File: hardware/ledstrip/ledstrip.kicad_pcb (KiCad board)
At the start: 4 copper layers, 98 parts, among them J1 Conn_ARM_JTAG_SWD_10, J2 USB_C_Receptacle_USB2.0_16P, J4 BMS connectors, J5 Ledstrip connector, J6 Header for STUSB4500 I2C, Q1 Q_NMOS, Q10 Q_PMOS, Q2 Q_NMOS, Q3 Q_NMOS, Q4 Q_PMOS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

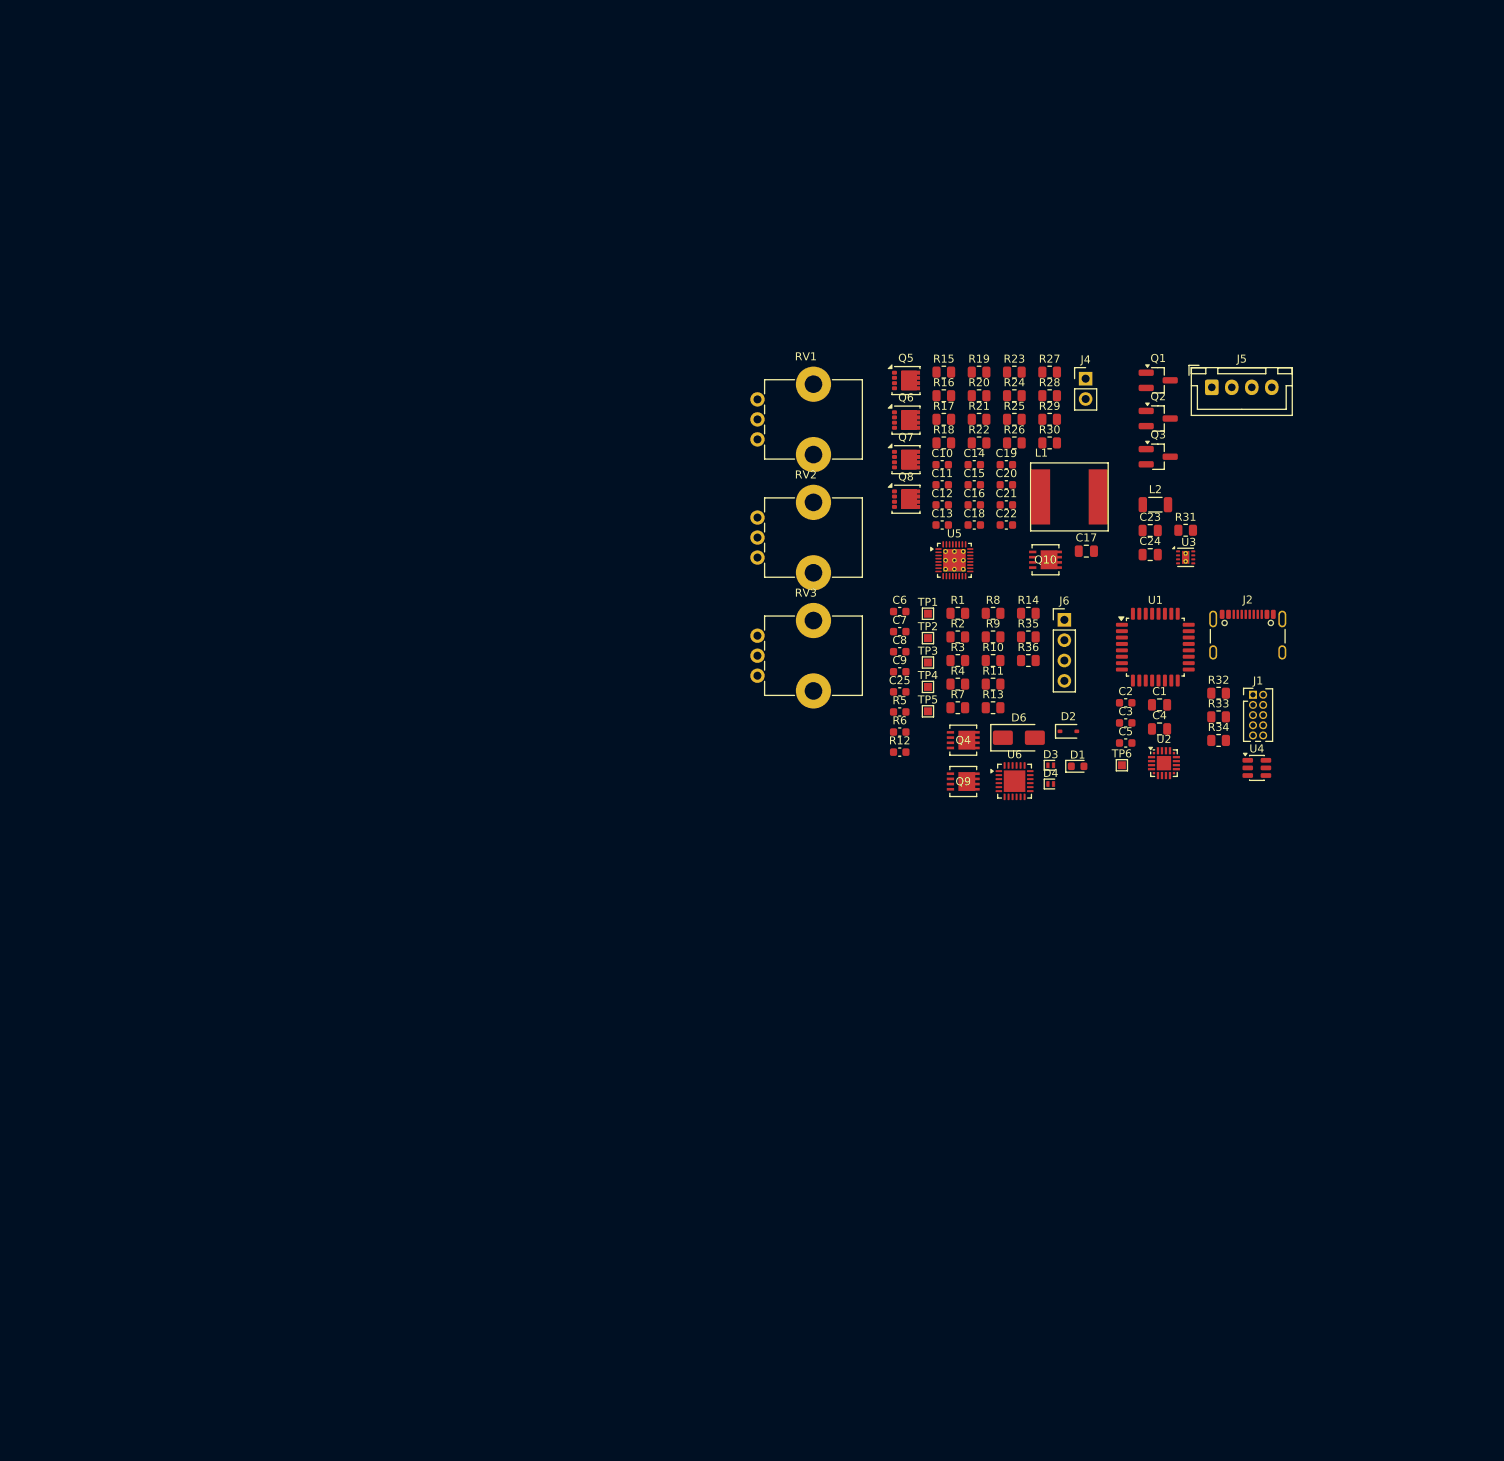
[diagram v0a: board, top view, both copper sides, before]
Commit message: Continue PCB.
Create netlists and color them.
Fix wrong symbol pin <-> foot print pins mapping.
Replace footprint and part for leds N-MOSFET.
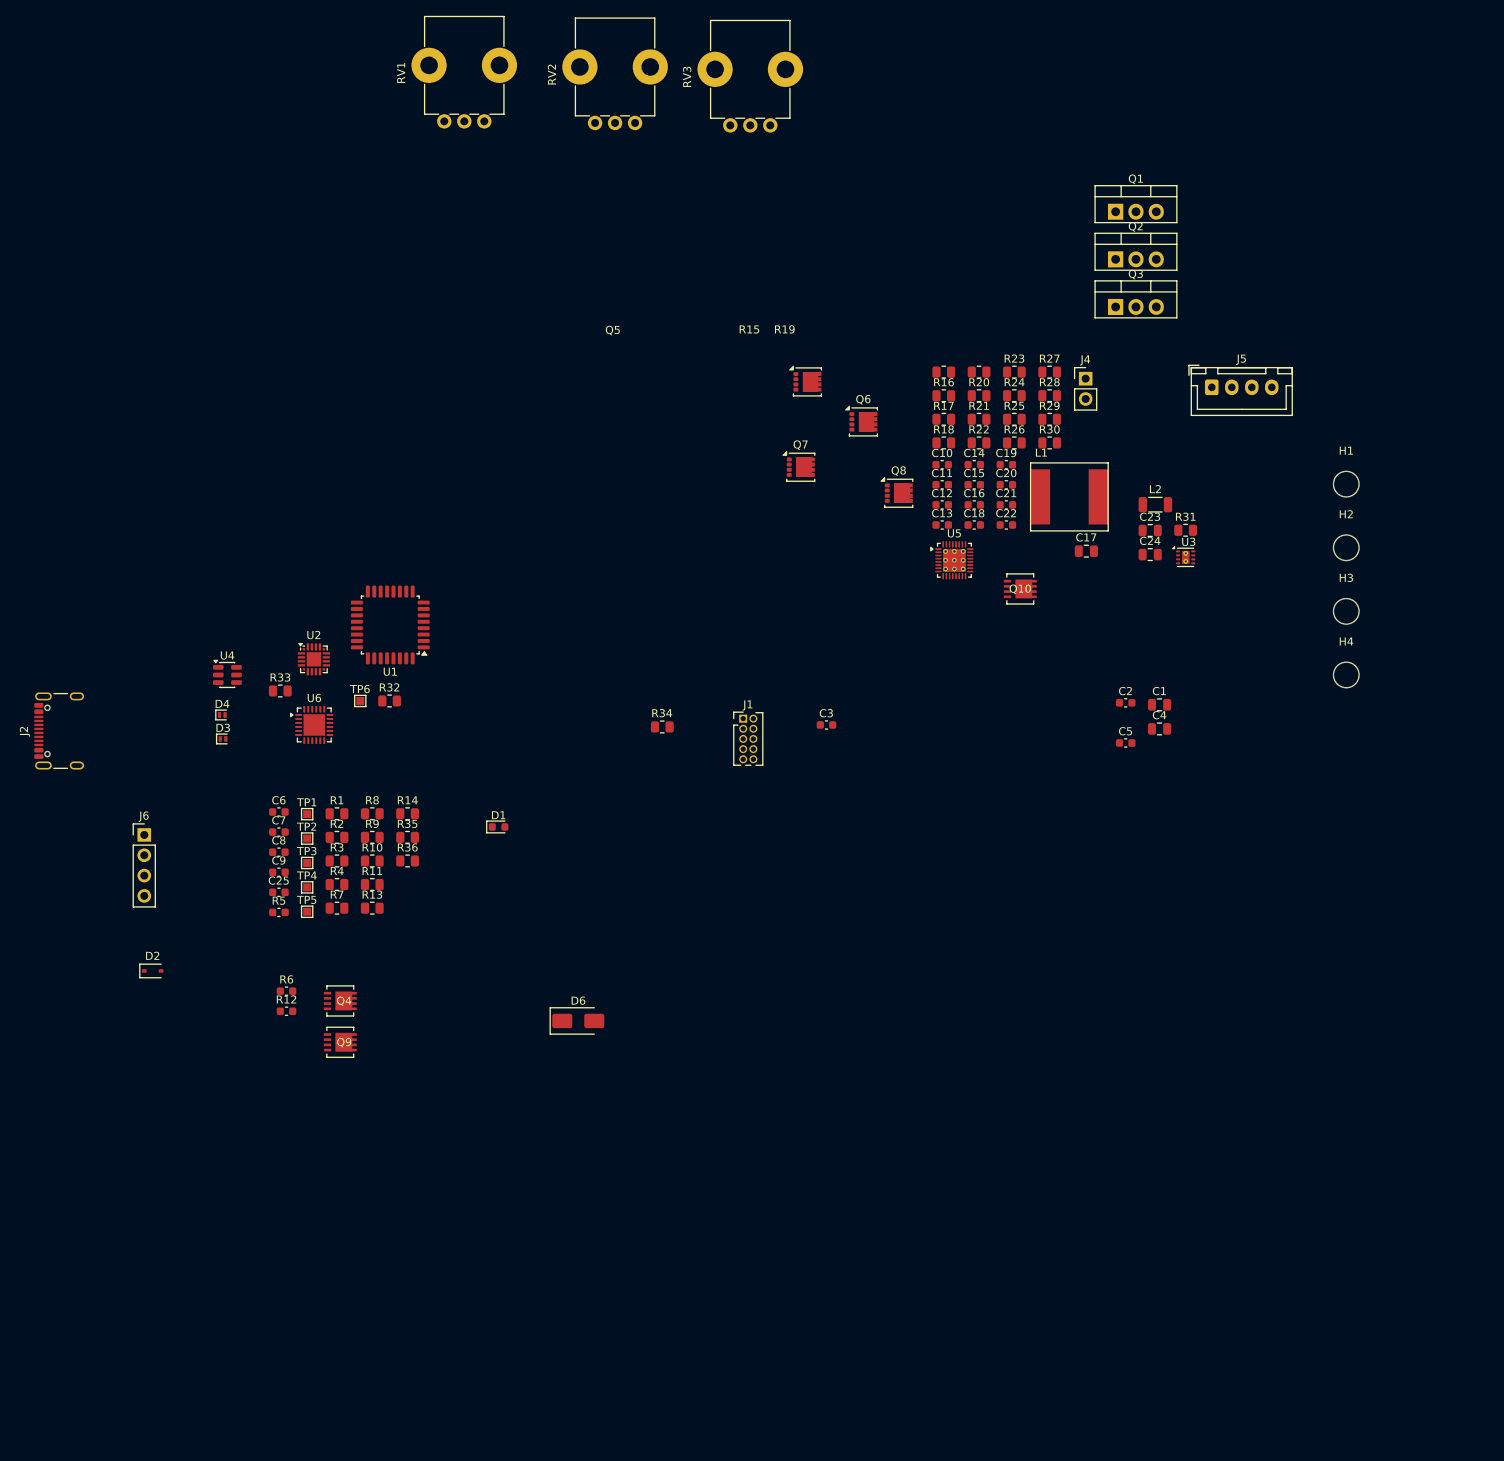
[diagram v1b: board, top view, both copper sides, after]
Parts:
- added H1: MountingHole, MountingHole:MountingHole_3.2mm_M3, F.Cu at (185.5, 76.2)
- added H2: MountingHole, MountingHole:MountingHole_3.2mm_M3, F.Cu at (185.5, 84.1)
- added H3: MountingHole, MountingHole:MountingHole_3.2mm_M3, F.Cu at (185.5, 92.0)
- added H4: MountingHole, MountingHole:MountingHole_3.2mm_M3, F.Cu at (185.5, 100.0)
- Q1, Q2, Q3: footprint Package_TO_SOT_SMD:SOT-23_Handsoldering -> TOT-220-3:TO-220-3_Vertical
- Q5, Q6, Q7, Q8: footprint Package_SON:VSON-8_3.3x3.3mm_P0.65mm_NexFET -> NexFET:VSON-8_3.3x3.3mm_P0.65mm_NexFET
- moved J2 147.8 mm to (25.8, 107.0), turned to 90 degrees
- moved U4 129.2 mm to (45.6, 100.0)
- moved D2 118.3 mm to (36.3, 137.0)
- moved J6 118.1 mm to (35.2, 120.0)
- moved R33 117.3 mm to (52.2, 102.0)
- moved U2 107.0 mm to (56.5, 98.0)
- moved D4 103.9 mm to (45.0, 105.0)
- moved R32 103.6 mm to (65.9, 103.2)
- moved D3 103.5 mm to (45.1, 108.0)
- moved U1 95.7 mm to (66.0, 93.8), turned to 180 degrees
- moved TP6 95.5 mm to (62.2, 103.2)
- moved U6 87.8 mm to (56.5, 106.2)
- moved Q9 84.4 mm to (59.8, 145.9)
- moved Q4 84.4 mm to (59.8, 140.8)
- moved R12 83.2 mm to (53.0, 142.0)
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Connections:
- net /STM32G0_RESET renamed /DBG_RESET
- net /STM32G0_SWDCLK renamed /DBG_SWDCLK
- net /STM32G0_SWDIO renamed /DBG_SWDIO
- net /USB PD/STUSB4500_I2C_SCL renamed /USB PD/STUSB4500_I2C_HEADER_SCL
- net /USB PD/STUSB4500_I2C_SDA renamed /USB PD/STUSB4500_I2C_HEADER_SDA
- net /USB PD/STUSB4500_I2C_VSYS renamed /USB PD/STUSB4500_I2C_HEADER_VSYS
- net /USB PD/USB_VBUS renamed /USB PD/VBUS
- net Net-(U2-VBUS) renamed /CP2102N_VBUS
- net Net-(U5-CELL_BATPRESZ) renamed /Battery Charger/BQ25703A_CELL_BATPRESZ
- net Net-(U5-PGND) renamed /Battery Charger/BQ25703A_PGND
- net Net-(U6-VREG_1V2) renamed /USB PD/STUSB4500_VREG_1V2
- net Net-(U6-VREG_2V7) renamed /USB PD/STUSB4500_VREG_2V7
- net Net-(U6-VSYS) renamed /USB PD/STUSB4500_VSYS
- C25 pad 1: /USB PD/STUSB4500_DISCH -> /Battery Charger/V_SNK
- C9 pad 2: Net-(U6-VDD) -> /USB PD/STUSB4500_VDD
- D1 pad 1: /USB PD/STUSB4500_DISCH -> /Battery Charger/V_SNK
- J2 pad A7: /USB_D+ -> /USB_D-
- J2 pad B7: /USB_D+ -> /USB_D-
- R12 pad 1: Net-(U6-DISCH) -> /USB PD/STUSB4500_DISCH
- R12 pad 2: /USB PD/STUSB4500_DISCH -> /Battery Charger/V_SNK
- R13 pad 1: Net-(U6-VDD) -> /USB PD/STUSB4500_VDD
- R16 pad 1: /USB PD/STUSB4500_DISCH -> /Battery Charger/V_SNK
- R18 pad 1: /USB PD/STUSB4500_DISCH -> /Battery Charger/V_SNK
- U4 pad 1: /USB_D+ -> /USB_D-
- U6 pad 24: Net-(U6-VDD) -> /USB PD/STUSB4500_VDD
- U6 pad 9: Net-(U6-DISCH) -> /USB PD/STUSB4500_DISCH

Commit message: Fix ILIM_HIZ setting on BQ25703A
Add comments on schematics about hardware configuration.
Setup a early stable 2.5V from REGN to setup ILIM_HIZ correctly.
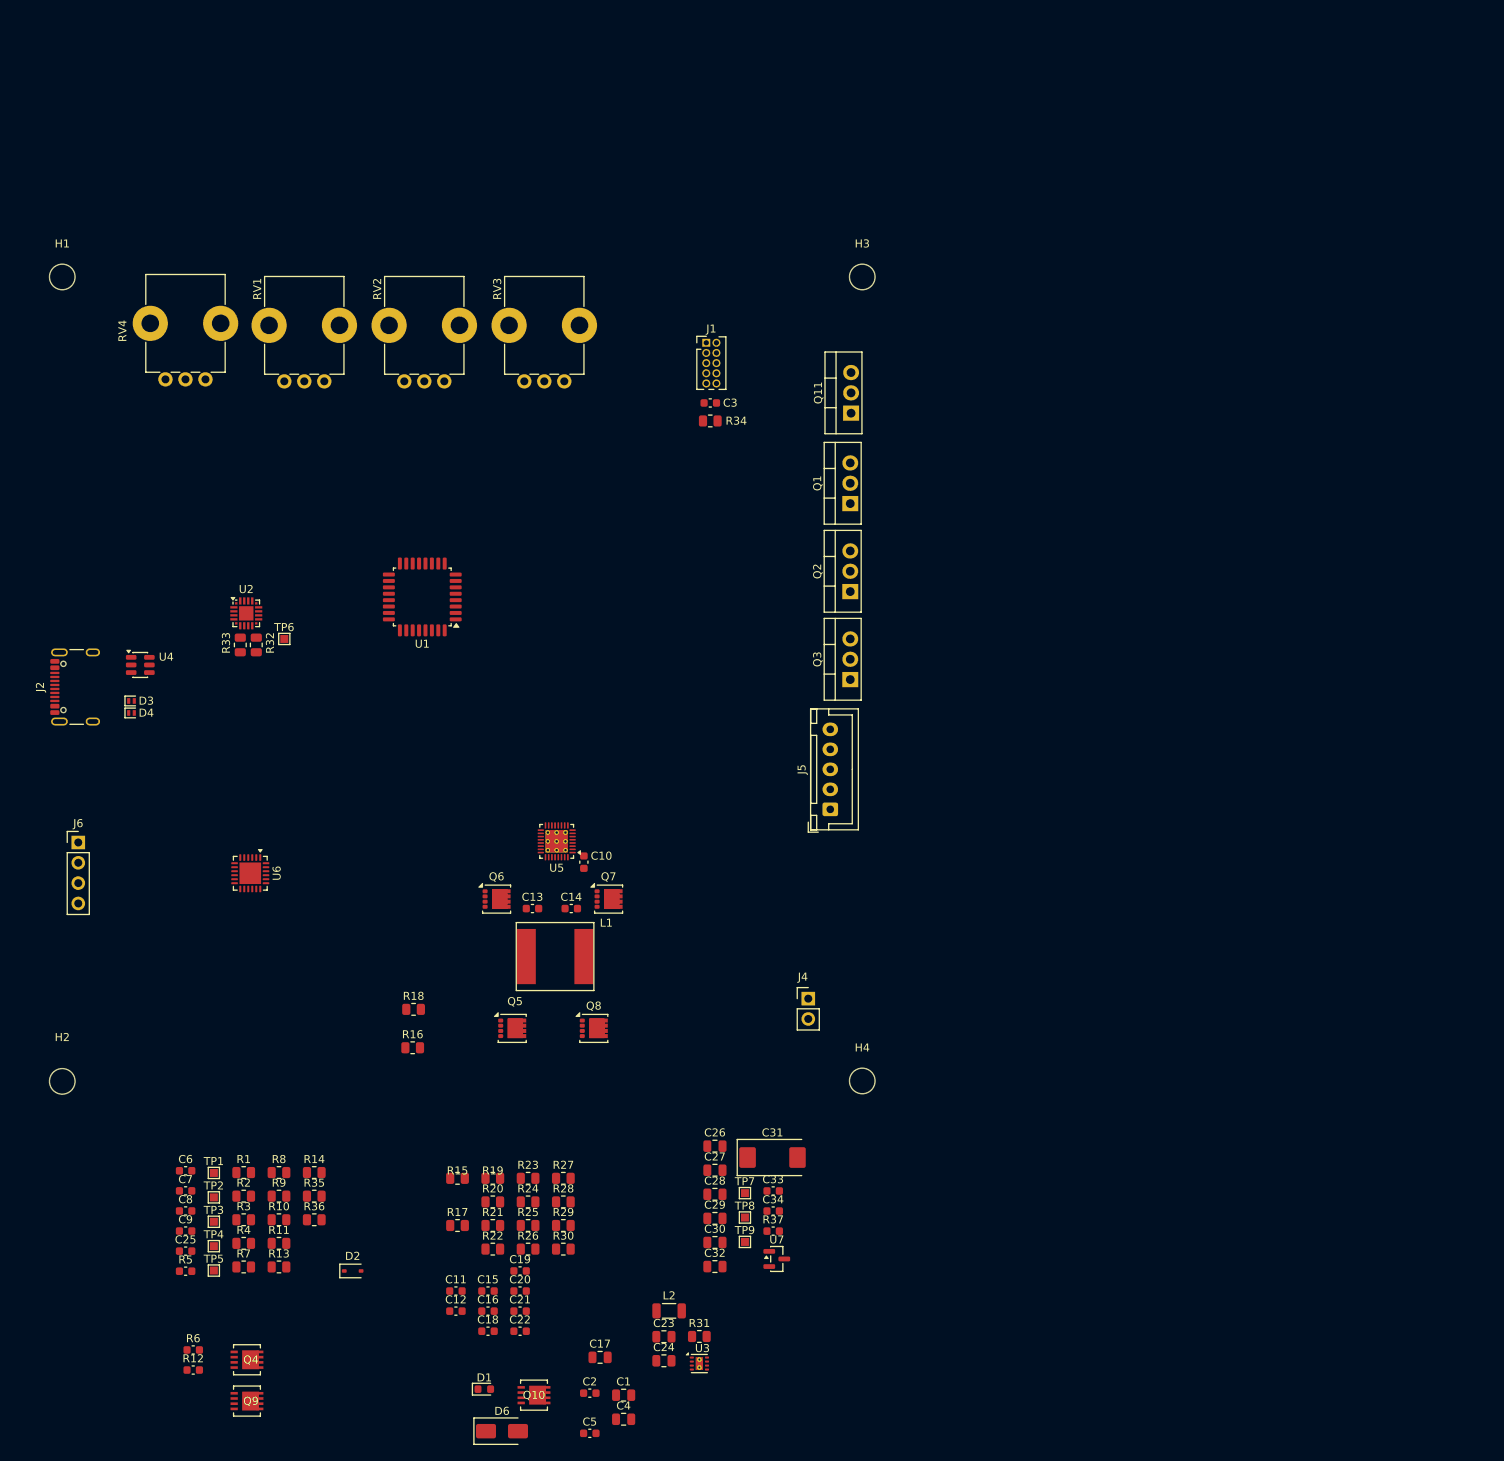
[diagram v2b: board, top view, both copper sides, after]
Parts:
- added C26: 10u, Capacitor_SMD:C_0805_2012Metric, F.Cu at (106.6, 158.9)
- added C27: 10u, Capacitor_SMD:C_0805_2012Metric, F.Cu at (106.6, 161.9)
- added C28: 10u, Capacitor_SMD:C_0805_2012Metric, F.Cu at (106.6, 164.9)
- added C29: 10u, Capacitor_SMD:C_0805_2012Metric, F.Cu at (106.6, 167.9)
- added C30: 10u, Capacitor_SMD:C_0805_2012Metric, F.Cu at (106.6, 170.9)
- added C31: 47u, Capacitor_Tantalum_SMD:CP_EIA-7343-20_Kemet-V, F.Cu at (113.8, 160.3)
- added C32: 10u, Capacitor_SMD:C_0805_2012Metric, F.Cu at (106.6, 173.9)
- added C33: 2.2u, Capacitor_SMD:C_0603_1608Metric, F.Cu at (113.9, 164.5)
- added C34: 1u, Capacitor_SMD:C_0603_1608Metric, F.Cu at (113.9, 167.0)
- added Q11: Q_NMOS, TOT-220-3:TO-220-3_Vertical, F.Cu at (123.6, 67.3)
- added R37: 1k, Capacitor_SMD:C_0603_1608Metric, F.Cu at (113.9, 169.5)
- added RV4: Pot_W, Potentiometer_THT:Potentiometer_Bourns_PTV09A-1_Single_Vertical, F.Cu at (42.9, 63.0)
- added TP7: TestPoint, TestPoint:TestPoint_Pad_1.0x1.0mm, F.Cu at (110.3, 164.8)
- added TP8: TestPoint, TestPoint:TestPoint_Pad_1.0x1.0mm, F.Cu at (110.3, 167.8)
- added TP9: TestPoint, TestPoint:TestPoint_Pad_1.0x1.0mm, F.Cu at (110.3, 170.9)
- added U7: TL431DBZ, Package_TO_SOT_SMD:SOT-23, F.Cu at (114.3, 173.0)
- C16: value 3.3uF -> 100nf
- J5: footprint Connector_JST:JST_XH_B4B-XH-A_1x04_P2.50mm_Vertical -> Connector_JST:JST_XH_B5B-XH-A_1x05_P2.50mm_Vertical
- R28: value 39K -> 107k
- moved H2 173.8 mm to (25.0, 150.8)
- moved H1 162.6 mm to (25.0, 50.2)
- moved C12 117.7 mm to (74.2, 179.5)
- moved C16 117.7 mm to (78.2, 179.5)
- moved C17 117.7 mm to (92.2, 185.3)
- moved C18 117.7 mm to (78.2, 182.0)
- moved C19 117.7 mm to (82.2, 174.5)
- moved C21 117.7 mm to (82.2, 179.5)
- moved C22 117.7 mm to (82.2, 182.0)
- moved C23 117.7 mm to (100.2, 182.7)
- moved Q10 117.7 mm to (84.0, 190.0)
- moved R20 117.7 mm to (78.8, 165.9)
- moved R22 117.7 mm to (78.8, 171.8)
- moved R24 117.7 mm to (83.2, 165.9)
- moved R26 117.7 mm to (83.2, 171.8)
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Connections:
- C16 pad 1: BQ25703A_REGN -> VREF_2V5
- C16 pad 2: /Battery Charger/BQ25703A_PGND -> GND
- R22 pad 1: BQ25703A_VDDA -> BQ25703A_REGN
- R22 pad 2: BQ25703A_REGN -> BQ25703A_VDDA
- R27 pad 1: BQ25703A_VDDA -> GND
- R28 pad 1: GND -> VREF_2V5
- U1 pad 10: unconnected-(U1-PA3-Pad10) -> /Pots/POT_W
- U1 pad 12: unconnected-(U1-PA5-Pad12) -> /leds/PWM_W
- U5 pad 27: /Battery Charger/BQ25703A_PGND -> GND
- U6 pad 21: /USB PD/STUSB4500_VREG_1V2 -> /USB PD/STUSB4500_VREG_2V7
- U6 pad 22: /USB PD/STUSB4500_VSYS -> /USB PD/STUSB4500_VDD
- U6 pad 23: /USB PD/STUSB4500_VREG_2V7 -> /USB PD/STUSB4500_VREG_1V2
- U6 pad 24: /USB PD/STUSB4500_VDD -> /USB PD/STUSB4500_VSYS
